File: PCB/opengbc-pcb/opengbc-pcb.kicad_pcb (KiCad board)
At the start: 2 copper layers, 70 x 122.2 mm, 80 parts, among them P1 CART_CONN, P2 DISP_FFC, P3 EXT_CONNECTOR, P4 Barrel_Jack_Switch, P5 AudioJack3_Switch, Q1 2SC4081UB, Q2 2SC4081UB, Q3 PT380F, Q4 2SC4081UB, SW1 PWR_SWITCH, U1 GameBoy_CPU_CGB_KF2007, U2 AS6C62256-55STIN, U3 LM4853, U4 TPS3840DL35, U6 Regulator board, U7 LD1117S33TR_SOT223, U8 gbc_buttons, Y1 SG-8018CE 8.388608M-TJHPA0

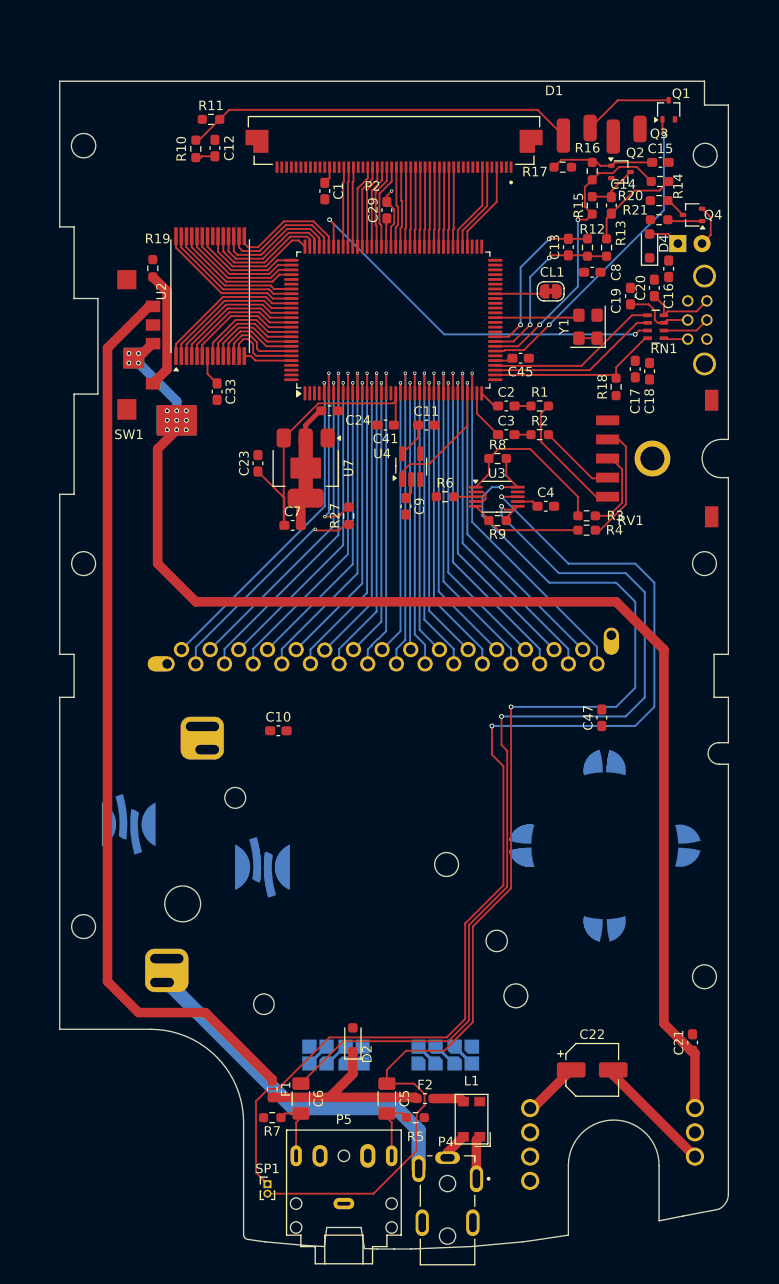
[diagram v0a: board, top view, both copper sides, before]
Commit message: update schematic
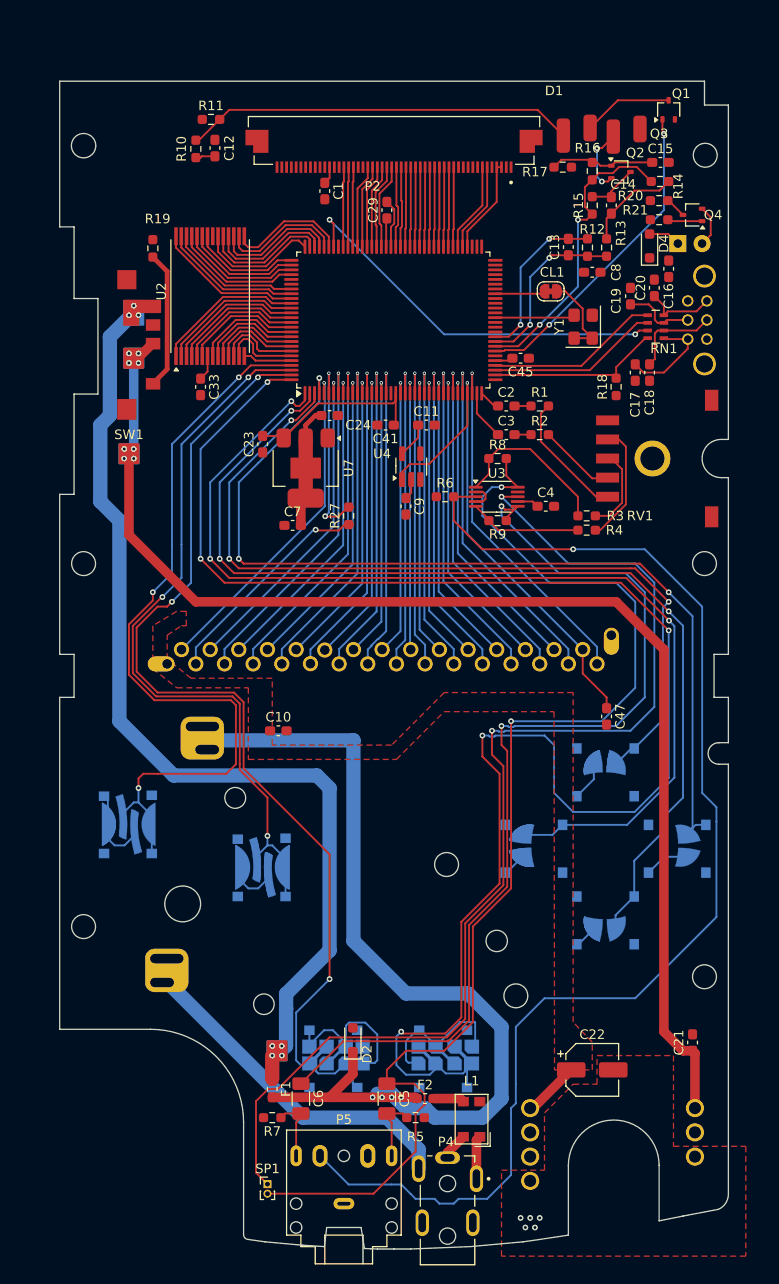
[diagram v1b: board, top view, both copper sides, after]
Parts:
- U8: value gbc_buttons -> Buttons
- moved R19 2.09 mm to (103.5, 50.0)
- moved C23 2.06 mm to (115.0, 70.5), turned to -90 degrees
- moved C33 1.80 mm to (108.5, 64.5)
- moved C47 0.52 mm to (151.0, 99.0), turned to -90 degrees
- moved C24 0.50 mm to (122.0, 67.5)
- moved Y1 0.50 mm to (148.6, 58.2)
- moved C17 0.36 mm to (154.0, 63.0)
- moved C18 0.14 mm to (155.5, 63.0)
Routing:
- net Net-(U1A-P12): track 0.00 -> 183.4 mm, vias 0 -> 5
- net Net-(U3-HP-IN): track 2.30 -> 132.4 mm, vias 0 -> 1
- net Net-(U1A-P13): track 0.00 -> 114.0 mm, vias 0 -> 3
- net Net-(U1A-P00): track 0.00 -> 108.5 mm, vias 0 -> 3
- net Net-(U1A-P03): track 0.00 -> 107.7 mm, vias 0 -> 3
- net Net-(U1A-P01): track 0.00 -> 99.7 mm, vias 0 -> 3
- net Net-(U1A-P02): track 0.00 -> 88.6 mm, vias 0 -> 3
- net Net-(U1A-P10): track 0.00 -> 82.2 mm, vias 0 -> 3
- net /Power/B+: track 21.0 -> 100.0 mm, vias 0 -> 4
- net Net-(U1A-P11): track 0.00 -> 77.7 mm, vias 0 -> 3
- net GND: track 21.9 -> 68.5 mm, vias 1 -> 5
- net +5V: track 45.7 -> 32.1 mm
- net Net-(P3-SCK): track 2.54 -> 10.4 mm
- net Net-(F1-Pad2): track 94.5 -> 102.2 mm, vias 0 -> 7
- net Net-(P1-~{RES}): track 47.1 -> 54.2 mm
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- added copper zone on F.Cu, net +5V
- added copper zone on F.Cu, net GND

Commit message: I HATE KICAD
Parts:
- U1: footprint Package_QFP:LQFP-128_14x20mm_P0.5mm -> gbc_repro_lib:LQFP-128_14x20mm_P0.5mm
- U8: value Buttons -> gbc_buttons
- Y1: value SG-8018CE 8.388608M-TJHPA0 -> SG-8018CG 8.388608M-TJHPA0
- moved C8 23.5 mm to (144.5, 75.5)
- moved R11 2.41 mm to (112.0, 36.5), turned to 90 degrees
- moved C11 0.64 mm to (131.5, 68.5)
- moved R3 0.50 mm to (148.9, 77.5)
- moved R4 0.50 mm to (148.9, 80.0)
- moved C4 0.14 mm to (144.5, 77.0)
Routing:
- net +5V: track 32.1 -> 251.4 mm, vias 0 -> 5
- net +3.3V: track 27.3 -> 135.0 mm, vias 0 -> 6
- net VCC: track 132.3 -> 193.2 mm, vias 8 -> 10
- net GND: track 68.5 -> 113.4 mm, vias 5 -> 98
- net Net-(U1A-P10): track 82.2 -> 80.4 mm
- net Net-(R4-Pad1): track 12.6 -> 14.1 mm
- net Net-(P1-~{RES}): track 54.2 -> 55.1 mm
- net Net-(U3-LEFT_IN): track 17.4 -> 16.9 mm
- added copper zone on B.Cu, net GND

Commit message: schematic or smth idk
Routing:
- net GND: vias 98 -> 106
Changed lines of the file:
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@@
+	)
+	(via
+		(at 126.5 96.5)
+		(size 0.6)
+		(drill 0.3)
+		(layers "F.Cu" "B.Cu")
+		(free yes)
+		(net 1)
 	)
 	(via
@@
 	)
 	(via
+		(at 104.5 99)
+		(size 0.6)
+		(drill 0.3)
+		(layers "F.Cu" "B.Cu")
+		(free yes)
+		(net 1)
+	)
+	(via
 		(at 130 38)
 		(size 0.6)
@@
 	)
 	(via
+		(at 104.5 100)
+		(size 0.6)
+		(drill 0.3)
+		(layers "F.Cu" "B.Cu")
+		(free yes)
+		(net 1)
+	)
+	(via
 		(at 134.5 53.5)
 		(size 0.6)
@@
 	)
 	(via
+		(at 126 97.5)
+		(size 0.6)
+		(drill 0.3)
+		(layers "F.Cu" "B.Cu")
+		(free yes)
+		(net 1)
+	)
+	(via
 		(at 125.5 58)
 		(size 0.6)
@@
 	)
 	(via
+		(at 125.5 96.5)
+		(size 0.6)
+		(drill 0.3)
+		(layers "F.Cu" "B.Cu")
+		(free yes)
+		(net 1)
+	)
+	(via
 		(at 115 73.5)
 		(size 0.6)
@@
 	)
 	(via
+		(at 127 97.5)
+		(size 0.6)
+		(drill 0.3)
+		(layers "F.Cu" "B.Cu")
+		(free yes)
+		(net 1)
+	)
+	(via
 		(at 124.5 40)
 		(size 0.6)
@@
 	)
 	(via
+		(at 127.5 96.5)
+		(size 0.6)
+		(drill 0.3)
+		(layers "F.Cu" "B.Cu")
+		(free yes)
+		(net 1)
+	)
+	(via
 		(at 123.5 58)
 		(size 0.6)
 		(drill 0.3)
+		(layers "F.Cu" "B.Cu")
+		(free yes)
+		(net 1)
+	)
+	(via
+		(at 103.5 99)
+		(size 0.6)
+		(drill 0.3)

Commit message: finish the thing
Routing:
- net GND: vias 106 -> 131
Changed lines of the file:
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@@
+	)
+	(via
+		(at 120.5 120.5)
+		(size 0.6)
+		(drill 0.3)
+		(layers "F.Cu" "B.Cu")
+		(free yes)
+		(net 1)
 	)
 	(via
@@
 	)
 	(via
+		(at 113.5 122.5)
+		(size 0.6)
+		(drill 0.3)
+		(layers "F.Cu" "B.Cu")
+		(free yes)
+		(net 1)
+	)
+	(via
 		(at 134.5 52.5)
 		(size 0.6)
@@
 	)
 	(via
+		(at 97.5 102)
+		(size 0.6)
+		(drill 0.3)
+		(layers "F.Cu" "B.Cu")
+		(free yes)
+		(net 1)
+	)
+	(via
 		(at 128.5 38)
 		(size 0.6)
@@
 	)
 	(via
+		(at 158.5 81.5)
+		(size 0.6)
+		(drill 0.3)
+		(layers "F.Cu" "B.Cu")
+		(free yes)
+		(net 1)
+	)
+	(via
 		(at 150.5 106.5)
 		(size 0.6)
@@
 	)
 	(via
+		(at 120.5 119)
+		(size 0.6)
+		(drill 0.3)
+		(layers "F.Cu" "B.Cu")
+		(free yes)
+		(net 1)
+	)
+	(via
 		(at 115 74.5)
 		(size 0.6)
@@
 	)
 	(via
+		(at 98 127)
+		(size 0.6)
+		(drill 0.3)
+		(layers "F.Cu" "B.Cu")
+		(free yes)
+		(net 1)
+	)
+	(via
 		(at 150.5 54.5)
 		(size 0.6)
@@
 	)
 	(via
+		(at 114.5 123.5)
+		(size 0.6)
+		(drill 0.3)
+		(layers "F.Cu" "B.Cu")
+		(free yes)
+		(net 1)
+	)
+	(via
 		(at 143 73.5)
 		(size 0.6)
@@
 	)
 	(via
+		(at 106.5 131)
+		(size 0.6)
+		(drill 0.3)
+		(layers "F.Cu" "B.Cu")
+		(free yes)
+		(net 1)
+	)
+	(via
+		(at 157.5 81.5)
+		(size 0.6)
+		(drill 0.3)
+		(layers "F.Cu" "B.Cu")
+		(free yes)
+		(net 1)
+	)
+	(via
 		(at 114 74.5)
 		(size 0.6)
@@
 	)
 	(via
+		(at 98 128)
+		(size 0.6)
+		(drill 0.3)
+		(layers "F.Cu" "B.Cu")
+		(free yes)
+		(net 1)
+	)
+	(via
+		(at 113.5 138)
+		(size 0.6)
+		(drill 0.3)
+		(layers "F.Cu" "B.Cu")
+		(free yes)
+		(net 1)
+	)
+	(via
+		(at 155 80.5)
+		(size 0.6)
+		(drill 0.3)
+		(layers "F.Cu" "B.Cu")
+		(free yes)
+		(net 1)
+	)
+	(via
 		(at 105 67.5)
 		(size 0.6)
@@
 	)
 	(via
+		(at 97.5 103)
+		(size 0.6)
+		(drill 0.3)
+		(layers "F.Cu" "B.Cu")
+		(free yes)
+		(net 1)
+	)
+	(via
 		(at 115 73.5)
 		(size 0.6)
@@
 	)
 	(via
+		(at 158.5 82.5)
+		(size 0.6)
+		(drill 0.3)
+		(layers "F.Cu" "B.Cu")
+		(free yes)
+		(net 1)
+	)
+	(via
 		(at 151 125)
 		(size 0.6)
@@
 	)
 	(via
+		(at 154 79.5)
+		(size 0.6)
+		(drill 0.3)
+		(layers "F.Cu" "B.Cu")
+		(free yes)
+		(net 1)
+	)
+	(via
+		(at 99 128)
+		(size 0.6)
+		(drill 0.3)
+		(layers "F.Cu" "B.Cu")
+		(free yes)
+		(net 1)
+	)
+	(via
 		(at 101 39)
 		(size 0.6)
@@
 	)
 	(via
+		(at 114.5 122.5)
+		(size 0.6)
+		(drill 0.3)
+		(layers "F.Cu" "B.Cu")
+		(free yes)
+		(net 1)
+	)
+	(via
+		(at 120.5 116)
+		(size 0.6)
+		(drill 0.3)
+		(layers "F.Cu" "B.Cu")
+		(free yes)
+		(net 1)
+	)
+	(via
 		(at 125.5 57)
 		(size 0.6)
@@
 	)
 	(via
+		(at 120.5 117.5)
+		(size 0.6)
+		(drill 0.3)
+		(layers "F.Cu" "B.Cu")
+		(free yes)
+		(net 1)
+	)
+	(via
 		(at 127 97.5)
 		(size 0.6)
@@
 	)
 	(via
+		(at 120.5 114.5)
+		(size 0.6)
+		(drill 0.3)
+		(layers "F.Cu" "B.Cu")
+		(free yes)
+		(net 1)
+	)
+	(via
+		(at 99 127)
+		(size 0.6)
+		(drill 0.3)
+		(layers "F.Cu" "B.Cu")
+		(free yes)
+		(net 1)
+	)
+	(via
 		(at 143 151.5)
 		(size 0.6)
@@
 	)
 	(via
+		(at 154 80.5)
+		(size 0.6)
+		(drill 0.3)
+		(layers "F.Cu" "B.Cu")
+		(free yes)
+		(net 1)
+	)
+	(via
 		(at 116 143.5)
 		(size 0.6)
@@
 	)
 	(via
+		(at 96.5 102)
+		(size 0.6)
+		(drill 0.3)
+		(layers "F.Cu" "B.Cu")
+		(free yes)
+		(net 1)
+	)
+	(via
 		(at 127.5 129.5)
 		(size 0.6)
@@
 	)
 	(via
+		(at 113.5 123.5)
+		(size 0.6)
+		(drill 0.3)
+		(layers "F.Cu" "B.Cu")
+		(free yes)
+		(net 1)
+	)
+	(via
 		(at 103.5 99)
 		(size 0.6)
@@
 		(size 0.6)
 		(drill 0.3)
+		(layers "F.Cu" "B.Cu")
+		(free yes)
+		(net 1)
+	)
+	(via
+		(at 96.5 103)
+		(size 0.6)
+		(drill 0.3)

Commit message: GROUND VIAS RAAAHHHHH also artwork n stuff
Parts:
- added G***: LOGO, gbc_repro_lib:artwork, F.Cu at (130.5, 113.5)
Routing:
- net GND: track 113.4 -> 124.6 mm, vias 131 -> 274
- net VCC: track 193.2 -> 197.3 mm
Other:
- board text added: "OpenGBC"
- board text added: "W?"

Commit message: make it more fun looking
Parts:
- added REF**: artwork2, gbc_repro_lib:artwork2, F.Cu at (101.0, 116.5)
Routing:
- net GND: vias 274 -> 285
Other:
- board text added: "A"
- board text added: "B"
- board text added: "B+"
- board text added: "B-"
- board text added: "CPU"
- board text added: "Cartridge slot"
- board text added: "Display Connector"
- board text added: "Down"
- board text added: "Left"
- board text added: "RAM"
- board text added: "Right"
- board text added: "Select"
- board text added: "Start"
- board text added: "Up"
- board text added: "VREG"
- board text added: "hello there :)"

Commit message: pcb minor updates
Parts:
- removed REF**: artwork2, gbc_repro_lib:artwork2
- added G***: artwork2, gbc_repro_lib:artwork2, F.Cu at (101.0, 116.5)
- moved C45 3.00 mm to (145.0, 61.5)
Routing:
- net GND: track 124.6 -> 131.6 mm, vias 285 -> 362
- net +5V: track 251.4 -> 254.4 mm
- net Net-(U1A-P13): track 114.0 -> 111.7 mm
- net VCC: track 197.3 -> 199.2 mm
- net Net-(U1A-P12): track 183.4 -> 184.6 mm
- net Net-(U1A-P00): track 108.5 -> 109.6 mm
- net Net-(U1A-P03): track 107.7 -> 108.5 mm
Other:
- board text added: "K"
- board text added: "SOC"
- board text removed: "CPU"

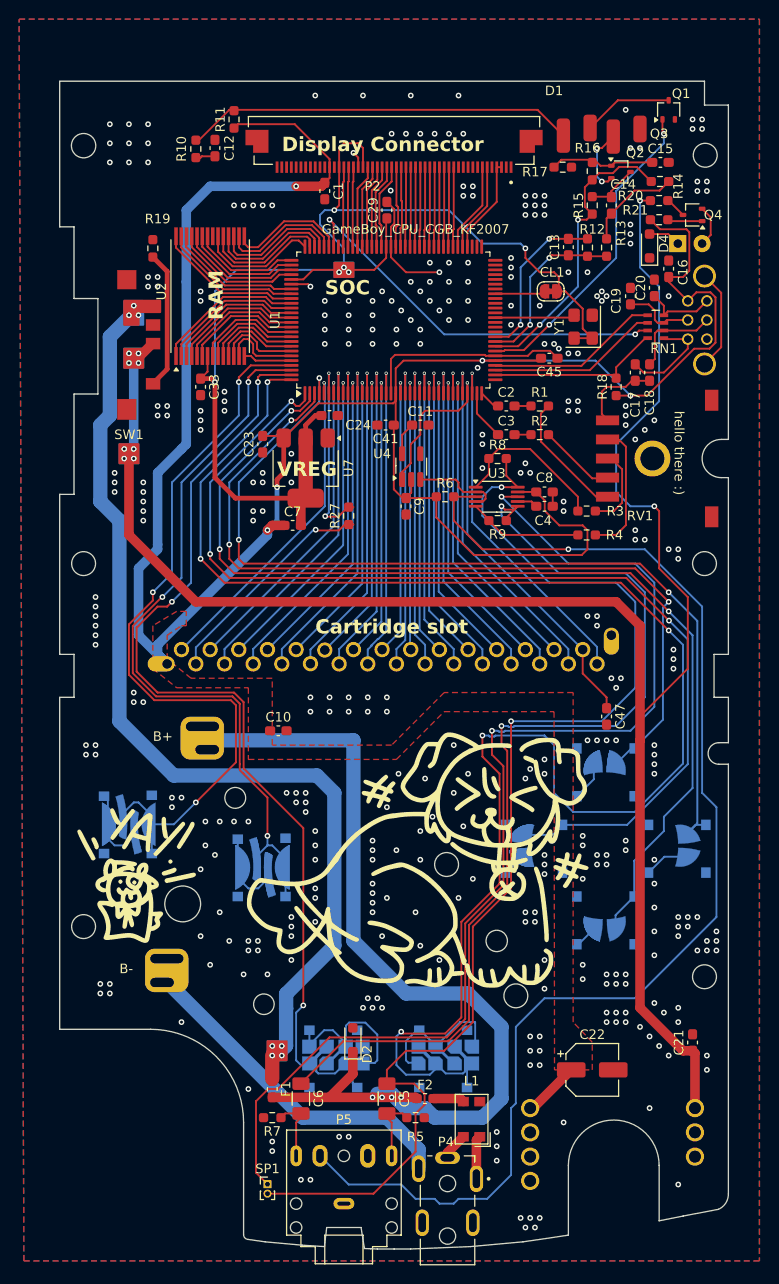
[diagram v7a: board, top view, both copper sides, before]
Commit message: update ground vias mostly and other pcb shenanigans
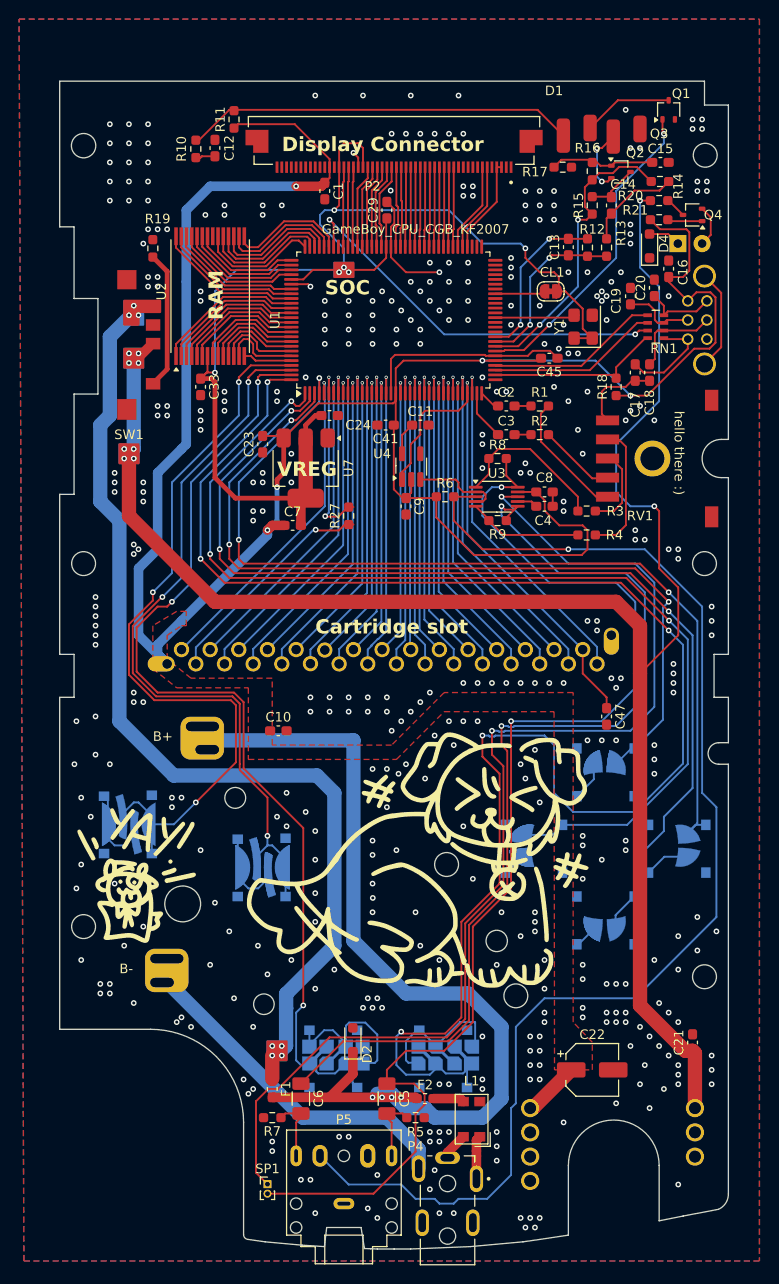
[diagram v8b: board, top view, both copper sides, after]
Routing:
- net VCC: track 199.2 -> 190.1 mm
- net Net-(U1B-~{WR}): track 20.7 -> 19.9 mm
- net Net-(P1-~{CS}): track 37.5 -> 36.6 mm
- net Net-(P1-VIN): track 37.9 -> 37.1 mm
- net Net-(P1-D7): track 37.1 -> 36.3 mm
- net Net-(P1-D5): track 36.3 -> 35.4 mm
- net Net-(P1-D3): track 35.5 -> 34.6 mm
- net Net-(P1-D1): track 34.6 -> 33.8 mm
- net Net-(P1-A9): track 33.4 -> 32.5 mm
- net Net-(P1-A7): track 34.2 -> 33.3 mm
- net Net-(P1-A5): track 35.0 -> 34.1 mm
- net Net-(P1-A3): track 35.8 -> 35.0 mm
- net Net-(P1-A15): track 33.8 -> 32.9 mm
- net Net-(P1-A13): track 33.0 -> 32.1 mm
- net Net-(P1-A11): track 32.9 -> 32.1 mm
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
